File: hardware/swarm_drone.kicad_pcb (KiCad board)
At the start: 4 copper layers, 0 parts

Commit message: feat(kicad): Initial pcb layout
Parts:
- added C1: 100n, Capacitor_SMD:C_0402_1005Metric, F.Cu at (147.5, 106.1)
- added C10: 100n, Capacitor_SMD:C_0402_1005Metric, F.Cu at (175.4, 82.0)
- added C11: 2u2, Capacitor_SMD:C_0402_1005Metric, F.Cu at (145.5, 107.5)
- added C12: 2u2, Capacitor_SMD:C_0402_1005Metric, F.Cu at (178.2, 76.1)
- added C13: 10u, Capacitor_SMD:C_0603_1608Metric, F.Cu at (126.1, 104.0)
- added C14: 100n, Capacitor_SMD:C_0402_1005Metric, F.Cu at (120.9, 103.7)
- added C15: 10u, Capacitor_SMD:C_0603_1608Metric, F.Cu at (126.1, 106.0)
- added C16: 10n, Capacitor_SMD:C_0402_1005Metric, F.Cu at (122.5, 107.5)
- added C17: 0.1u, Capacitor_SMD:C_0402_1005Metric, F.Cu at (153.0, 95.2)
- added C18: 2.2u, Capacitor_SMD:C_0402_1005Metric, F.Cu at (154.1, 97.5)
- added C19: 10n, Capacitor_SMD:C_0402_1005Metric, F.Cu at (152.0, 95.2)
- added C2: 100n, Capacitor_SMD:C_0402_1005Metric, F.Cu at (173.0, 87.5)
- added C20: 100n, Capacitor_SMD:C_0402_1005Metric, F.Cu at (131.5, 103.0)
- added C21: 100n, Capacitor_SMD:C_0402_1005Metric, F.Cu at (133.7, 104.9)
- added C22: 26p, Capacitor_SMD:C_0402_1005Metric, F.Cu at (178.2, 78.0)
- added C23: 26p, Capacitor_SMD:C_0402_1005Metric, F.Cu at (178.2, 80.0)
- added C24: 100n, Capacitor_SMD:C_0402_1005Metric, B.Cu at (142.1, 101.6)
- added C25: 4u7, Capacitor_SMD:C_0603_1608Metric, B.Cu at (139.1, 99.5)
- added C26: 100n, Capacitor_SMD:C_0402_1005Metric, B.Cu at (144.6, 109.6)
- added C27: 4u7, Capacitor_SMD:C_0603_1608Metric, B.Cu at (146.1, 107.5)
- added C28: 33n, Capacitor_SMD:C_0402_1005Metric, F.Cu at (148.9, 71.0)
- added C29: 10n, Capacitor_SMD:C_0402_1005Metric, F.Cu at (148.9, 73.0)
- added C3: 100n, Capacitor_SMD:C_0402_1005Metric, F.Cu at (173.0, 89.5)
- added C30: 1n, Capacitor_SMD:C_0402_1005Metric, F.Cu at (141.0, 85.2)
- added C31: 2n2, Capacitor_SMD:C_0402_1005Metric, F.Cu at (151.7, 71.0)
- added C32: 4p7, Capacitor_SMD:C_0402_1005Metric, F.Cu at (151.7, 73.0)
- added C33: 1p5, Capacitor_SMD:C_0402_1005Metric, F.Cu at (151.0, 76.0)
- added C34: 1p, Capacitor_SMD:C_0402_1005Metric, F.Cu at (154.6, 71.0)
- added C35: 8p2, Capacitor_SMD:C_0402_1005Metric, F.Cu at (154.6, 73.0)
- added C36: 8p2, Capacitor_SMD:C_0402_1005Metric, F.Cu at (154.6, 74.9)
- added C4: 100n, Capacitor_SMD:C_0402_1005Metric, F.Cu at (173.0, 91.4)
- added C5: 100n, Capacitor_SMD:C_0402_1005Metric, F.Cu at (173.0, 93.4)
- added C6: 10u, Capacitor_SMD:C_0603_1608Metric, F.Cu at (182.2, 96.5)
- added C7: 10n, Capacitor_SMD:C_0402_1005Metric, F.Cu at (175.4, 76.1)
- added C8: 1u, Capacitor_SMD:C_0402_1005Metric, F.Cu at (175.4, 78.0)
- added C9: 1u, Capacitor_SMD:C_0402_1005Metric, F.Cu at (175.4, 80.0)
- added D1: D_Schottky, Diode_SMD:D_MicroSMP_LargeCathode, B.Cu at (127.0, 83.0)
- added D10: LED, LED_SMD:LED_0603_1608Metric, F.Cu at (154.5, 113.5)
- added D2: D_Schottky, Diode_SMD:D_MicroSMP_LargeCathode, B.Cu at (158.5, 82.1)
- added D3: D_Schottky, Diode_SMD:D_MicroSMP_LargeCathode, B.Cu at (126.0, 121.9)
- added D4: D_Schottky, Diode_SMD:D_MicroSMP_LargeCathode, B.Cu at (159.0, 121.4)
- added D5: LED, LED_SMD:LED_0603_1608Metric, F.Cu at (154.5, 103.5)
- added D6: LED, LED_SMD:LED_0603_1608Metric, F.Cu at (154.5, 105.5)
- added D7: LED, LED_SMD:LED_0603_1608Metric, F.Cu at (154.5, 107.5)
- added D8: LED, LED_SMD:LED_0603_1608Metric, F.Cu at (154.5, 109.5)
- added D9: LED, LED_SMD:LED_0603_1608Metric, F.Cu at (154.5, 111.5)
- added DWM1: DWM3000, RF_Module:DWM1000, F.Cu at (142.5, 122.0)
- added FB1: 120R, Inductor_SMD:L_0603_1608Metric, F.Cu at (182.2, 99.0)
- added J1: Conn_01x02_Pin, Connector_JST:JST_PH_S2B-PH-K_1x02_P2.00mm_Horizontal, B.Cu at (121.5, 100.5)
- added J2: Conn_01x03_Socket, Connector_PinHeader_1.00mm:PinHeader_1x03_P1.00mm_Horizontal, F.Cu at (163.0, 100.5)
- added J3: Conn_01x03_Socket, Connector_PinHeader_1.00mm:PinHeader_1x03_P1.00mm_Horizontal, F.Cu at (163.0, 96.5)
- added J5: Conn_01x02_Socket, Connector_JST:JST_ZH_B2B-ZR_1x02_P1.50mm_Vertical, B.Cu at (122.5, 81.8)
- added J6: Conn_01x02_Socket, Connector_JST:JST_ZH_B2B-ZR_1x02_P1.50mm_Vertical, B.Cu at (162.0, 81.5)
- added J7: Conn_01x02_Socket, Connector_JST:JST_ZH_B2B-ZR_1x02_P1.50mm_Vertical, B.Cu at (162.1, 120.8)
- added J8: Conn_01x02_Socket, Connector_JST:JST_ZH_B2B-ZR_1x02_P1.50mm_Vertical, B.Cu at (122.0, 120.8)
- added JP1: Jumper_2_Open, Jumper:SolderJumper-2_P1.3mm_Open_RoundedPad1.0x1.5mm, B.Cu at (138.0, 94.3)
- added JP2: Jumper_2_Open, Jumper:SolderJumper-2_P1.3mm_Open_RoundedPad1.0x1.5mm, B.Cu at (140.5, 94.3)
- added JP3: Jumper_2_Open, Jumper:SolderJumper-2_P1.3mm_Open_RoundedPad1.0x1.5mm, B.Cu at (143.0, 94.3)
- added JP4: Jumper_2_Open, Jumper:SolderJumper-2_P1.3mm_Open_RoundedPad1.0x1.5mm, B.Cu at (145.5, 94.3)
- added JP5: Jumper_2_Open, Jumper:SolderJumper-2_P1.3mm_Open_RoundedPad1.0x1.5mm, B.Cu at (148.0, 94.3)
- added JP6: Jumper_2_Open, Jumper:SolderJumper-2_P1.3mm_Open_RoundedPad1.0x1.5mm, B.Cu at (135.5, 94.3)
- added L1: 2n7, Inductor_SMD:L_0402_1005Metric, F.Cu at (157.5, 71.0)
- added L2: 3n9, Inductor_SMD:L_0402_1005Metric, F.Cu at (157.5, 73.0)
- added L3: 8n2, Inductor_SMD:L_0402_1005Metric, F.Cu at (157.5, 75.0)
- added Q1: AO3400A, Package_TO_SOT_SMD:SOT-23, B.Cu at (123.0, 87.5)
- added Q2: AO3400A, Package_TO_SOT_SMD:SOT-23, B.Cu at (162.7, 87.1)
- added Q3: AO3400A, Package_TO_SOT_SMD:SOT-23, B.Cu at (162.5, 116.5)
- added Q4: AO3400A, Package_TO_SOT_SMD:SOT-23, B.Cu at (122.5, 116.5)
- added R1: 10k, Resistor_SMD:R_0402_1005Metric, F.Cu at (139.1, 71.0)
- added R10: 2k2, Resistor_SMD:R_0402_1005Metric, F.Cu at (142.0, 71.0)
- added R11: 2k2, Resistor_SMD:R_0402_1005Metric, F.Cu at (150.0, 89.0)
- added R12: 10k, Resistor_SMD:R_0402_1005Metric, B.Cu at (126.0, 87.5)
- added R13: 10k, Resistor_SMD:R_0402_1005Metric, B.Cu at (160.0, 87.0)
- added R14: 10k, Resistor_SMD:R_0402_1005Metric, B.Cu at (159.5, 117.0)
- added R15: 10k, Resistor_SMD:R_0402_1005Metric, B.Cu at (125.0, 117.5)
- added R16: 10k, Resistor_SMD:R_0402_1005Metric, B.Cu at (140.1, 101.7)
- added R17: 10k, Resistor_SMD:R_0402_1005Metric, B.Cu at (144.0, 101.6)
- added R18: 10k, Resistor_SMD:R_0402_1005Metric, B.Cu at (141.1, 110.2)
- added R19: 10k, Resistor_SMD:R_0402_1005Metric, B.Cu at (134.6, 105.9)
- added R2: 10k, Resistor_SMD:R_0402_1005Metric, F.Cu at (139.1, 73.0)
- added R20: 22K, Resistor_SMD:R_0402_1005Metric, F.Cu at (116.0, 95.5)
- added R21: 100k, Resistor_SMD:R_0402_1005Metric, F.Cu at (179.6, 112.0)
- added R22: 330R, Resistor_SMD:R_0402_1005Metric, F.Cu at (157.0, 103.5)
- added R23: 330R, Resistor_SMD:R_0402_1005Metric, F.Cu at (157.0, 105.5)
- added R24: 330R, Resistor_SMD:R_0402_1005Metric, F.Cu at (157.0, 107.5)
- added R25: 330R, Resistor_SMD:R_0402_1005Metric, F.Cu at (157.0, 109.5)
- added R26: 330R, Resistor_SMD:R_0402_1005Metric, F.Cu at (157.0, 111.5)
- added R27: 330R, Resistor_SMD:R_0402_1005Metric, F.Cu at (157.0, 113.5)
- added R3: 3.57k, Resistor_SMD:R_0402_1005Metric, F.Cu at (124.5, 107.5)
- added R4: 1.15k, Resistor_SMD:R_0402_1005Metric, F.Cu at (124.5, 108.6)
- added R5: 10k, Resistor_SMD:R_0402_1005Metric, F.Cu at (124.4, 101.4)
- added R6: 33k, Resistor_SMD:R_0402_1005Metric, F.Cu at (124.4, 102.5)
- added R7: 10k, Resistor_SMD:R_0402_1005Metric, F.Cu at (149.9, 96.9)
- added R8: 2k2, Resistor_SMD:R_0402_1005Metric, B.Cu at (143.3, 97.4)
- added R9: 2k2, Resistor_SMD:R_0402_1005Metric, B.Cu at (141.3, 97.4)
- added SW1: SW_Push, Button_Switch_SMD:SW_Push_1P1T_NO_CK_KSC6xxG, F.Cu at (112.0, 110.5)
- added TP1: GND, TestPoint:TestPoint_Pad_D1.5mm, F.Cu at (169.3, 76.8)
- added TP2: I2C2_SCL, TestPoint:TestPoint_Pad_D1.5mm, F.Cu at (169.3, 80.4)
- added TP3: I2C2_SDA, TestPoint:TestPoint_Pad_D1.5mm, F.Cu at (169.3, 84.0)
- added TP4: +3V3, TestPoint:TestPoint_Pad_D1.5mm, F.Cu at (169.0, 87.5)
- added U1: STM32F405RGT7, Package_QFP:LQFP-64_10x10mm_P0.5mm, F.Cu at (142.3, 100.2)
- added U2: TPS7A91, Package_DFN_QFN:Texas_S-PDSO-N10_EP1.2x2mm, F.Cu at (123.0, 105.0)
- added U3: ICM-42688-P, ICM-42688-P:PQFN50P300X250X97-14N, F.Cu at (152.0, 98.0)
- added U4: BMP581, footprints:QFN10_BMP581_BOS, F.Cu at (133.5, 103.0)
- added U5: VL53L1CXV0FY1, Sensor_Distance:ST_VL53L1x, B.Cu at (142.7, 99.5)
- added U6: GD25Q128ESIGR, GD25Q128:SOP8_208MIL_GDV, B.Cu at (140.5, 106.5)
- added U7: nRF24L01P, Package_DFN_QFN:QFN-20-1EP_4x4mm_P0.5mm_EP2.5x2.5mm, F.Cu at (142.0, 88.5)
- added U8: NRF24L01_Breakout, RF_Module:nRF24L01_Breakout, B.Cu at (115.6, 70.3)
- added X1: 8MHz, abm:ABM3B_ABR, F.Cu at (133.3, 96.8)
- added Y1: 16MHz (C13738), Crystal:Crystal_SMD_3225-4Pin_3.2x2.5mm, F.Cu at (146.5, 88.0)
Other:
- board outline added: 45 x 45 mm

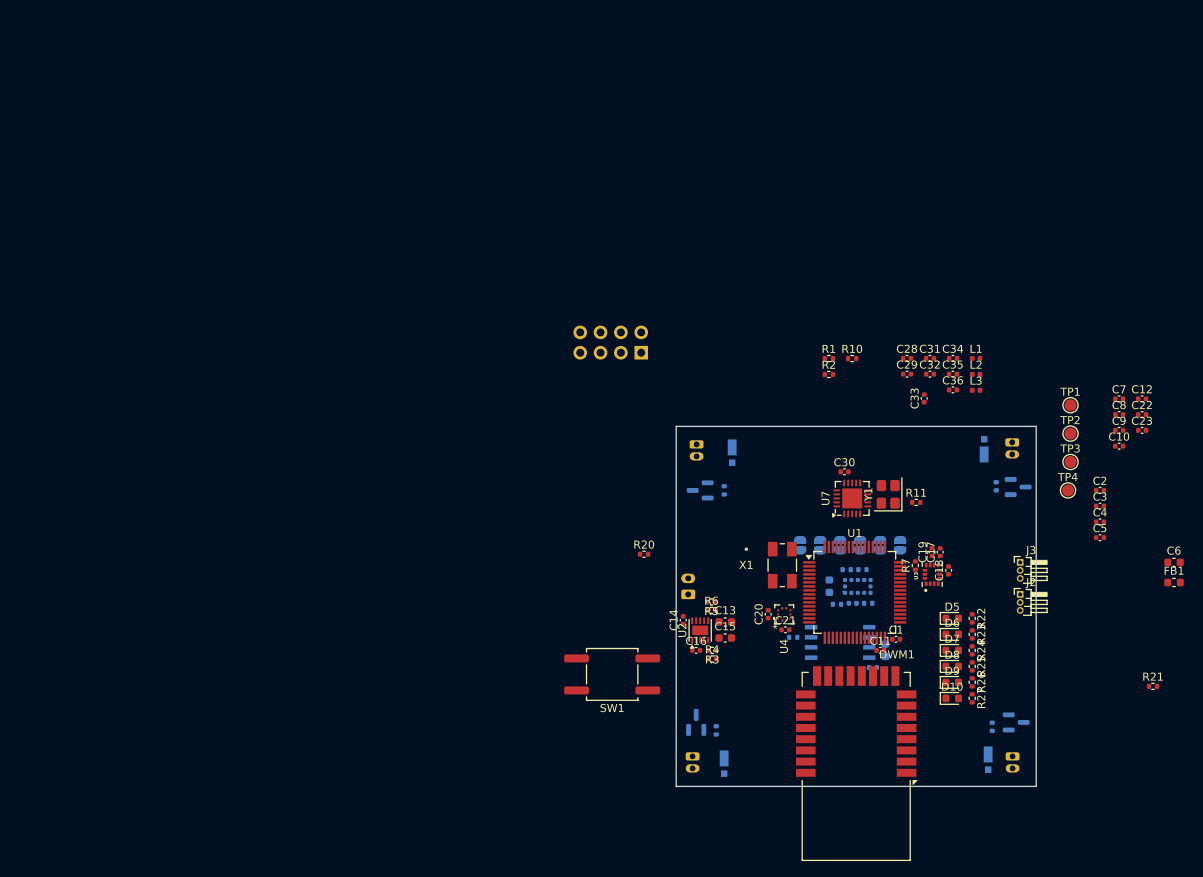
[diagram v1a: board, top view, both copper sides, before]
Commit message: feat(kicad): Added step files for missing parts
changed flyback diode to SMA part with 5A max

Redid initial layout
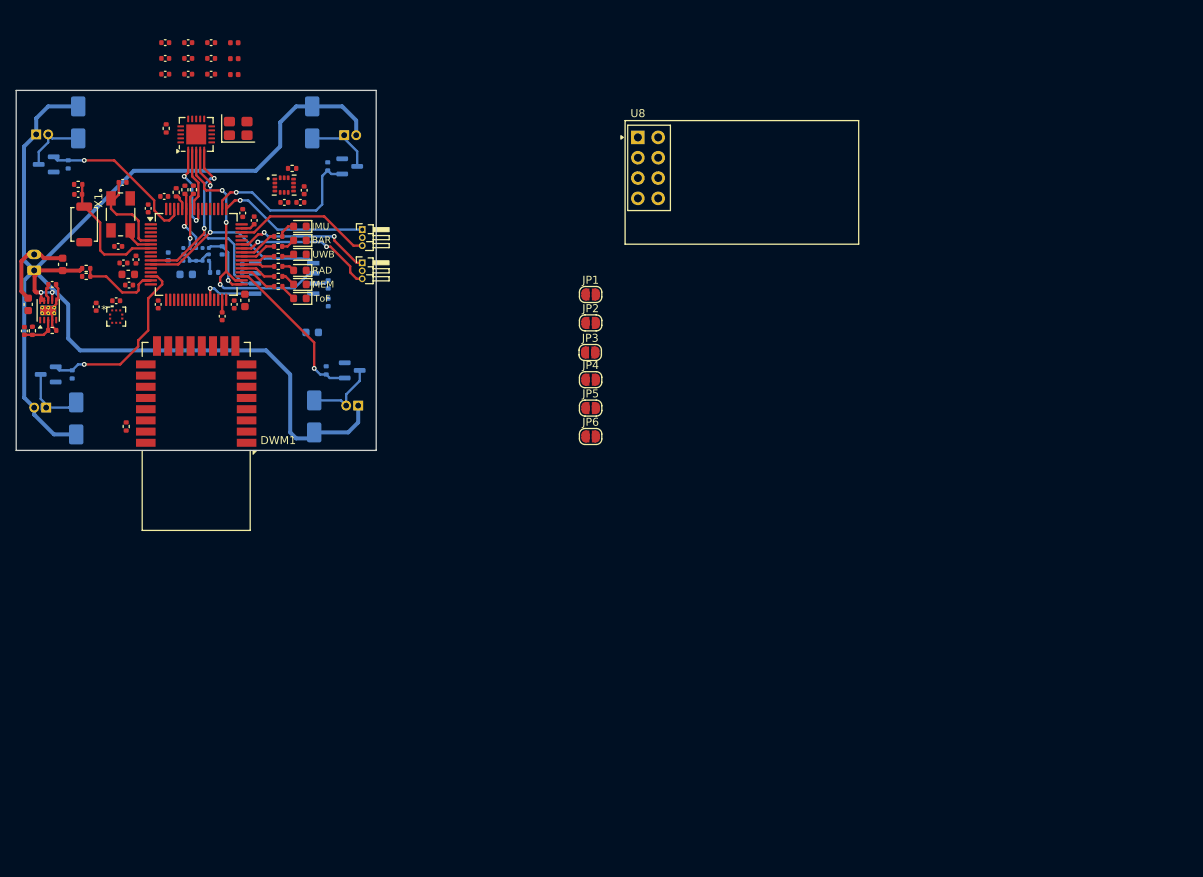
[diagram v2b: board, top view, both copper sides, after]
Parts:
- removed R10, R11: 2k2, Resistor_SMD:R_0402_1005Metric
- removed TP1: GND, TestPoint:TestPoint_Pad_D1.5mm
- removed TP2: I2C2_SCL, TestPoint:TestPoint_Pad_D1.5mm
- removed TP3: I2C2_SDA, TestPoint:TestPoint_Pad_D1.5mm
- removed TP4: +3V3, TestPoint:TestPoint_Pad_D1.5mm
- D1, D2, D3, D4: value D_Schottky -> D_Schottky (C22452); footprint Diode_SMD:D_MicroSMP_LargeCathode -> Diode_SMD:D_SMA
- J5, J6, J7, J8: footprint Connector_JST:JST_ZH_B2B-ZR_1x02_P1.50mm_Vertical -> MotorJST:JST_S2B-ZR-3.4_LF__SN_
- JP1, JP2, JP3, JP4, JP5, JP6, R8, R9, U8: moved to F.Cu
- SW1: footprint Button_Switch_SMD:SW_Push_1P1T_NO_CK_KSC6xxG -> Button_Switch_SMD:SW_SPST_TS-1088-xR020
- U2: footprint Package_DFN_QFN:Texas_S-PDSO-N10_EP1.2x2mm -> Package_DFN_QFN:Texas_S-PDSO-N10_EP1.2x2mm_ThermalVias
- moved FB1 136.3 mm to (51.5, 60.5), turned to 180 degrees
- moved C10 133.9 mm to (45.2, 50.5), turned to 180 degrees
- moved R21 132.4 mm to (51.2, 79.5), turned to -90 degrees
- moved C22 130.7 mm to (50.8, 49.0)
- moved C23 130.0 mm to (50.2, 57.0)
- moved C7 125.6 mm to (50.9, 59.1), turned to 180 degrees
- moved C9 125.1 mm to (51.6, 61.8), turned to 180 degrees
- moved C8 124.4 mm to (52.5, 58.6), turned to 90 degrees
- moved C4 123.9 mm to (56.0, 50.8)
- moved D4 121.8 mm to (45.0, 78.5), turned to 90 degrees
- moved C6 120.7 mm to (66.1, 63.8), turned to -90 degrees
- moved C2 120.0 mm to (55.2, 64.2), turned to 90 degrees
- moved C3 113.3 mm to (65.8, 52.8), turned to 90 degrees
- moved C12 113.2 mm to (67.2, 53.8), turned to -90 degrees
- moved C5 112.1 mm to (64.8, 64.2), turned to -90 degrees
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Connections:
- net Net-(U2-NR/SS) renamed /Power Regulation/NRSS
- C16 pad 1: +3V3 -> /Power Regulation/FB
- R3 pad 1: Net-(U2-FB) -> /Power Regulation/FB
- R4 pad 2: Net-(U2-FB) -> /Power Regulation/FB
- U1 pad 29: /Microcontroller/I2C2_SCL -> unconnected-(U1-PB10-Pad29)
- U1 pad 30: /Microcontroller/I2C2_SDA -> unconnected-(U1-PB11-Pad30)
- U2 pad 3: Net-(U2-FB) -> /Power Regulation/FB
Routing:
- net +BATT: track 0.00 -> 177.8 mm, vias 0 -> 2
- net /Barometer/SPI2_SCK: track 0.00 -> 34.8 mm, vias 0 -> 3
- net /Barometer/SPI2_MOSI: track 0.00 -> 34.4 mm, vias 0 -> 2
- net /Barometer/SPI2_MISO: track 0.00 -> 32.0 mm, vias 0 -> 2
- net /Microcontroller/M4: track 0.00 -> 22.8 mm, vias 0 -> 1
- net /Microcontroller/M2: track 0.00 -> 21.7 mm, vias 0 -> 1
- net GND: track 0.00 -> 21.5 mm
- net /Microcontroller/M1: track 0.00 -> 20.2 mm, vias 0 -> 1
- net /Microcontroller/M3: track 0.00 -> 20.0 mm, vias 0 -> 1
- net /Microcontroller/SWCLK: track 0.00 -> 19.0 mm, vias 0 -> 1
- net /Microcontroller/USART1_TX: track 0.00 -> 17.8 mm, vias 0 -> 2
- net /Microcontroller/USART1_RX: track 0.00 -> 17.6 mm, vias 0 -> 2
- net /Microcontroller/SWDIO: track 0.00 -> 17.4 mm
- net /Microcontroller/NRST: track 0.00 -> 15.8 mm
- net /Microcontroller/HSE_IN: track 0.00 -> 11.4 mm
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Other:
- board text added: "BAR"
- board text added: "IMU"
- board text added: "MEM"
- board text added: "RAD"
- board text added: "ToF"
- board text added: "UWB"

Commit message: feat(kicad): Updated schematic to keep traces shorter on the layout Restarting layout
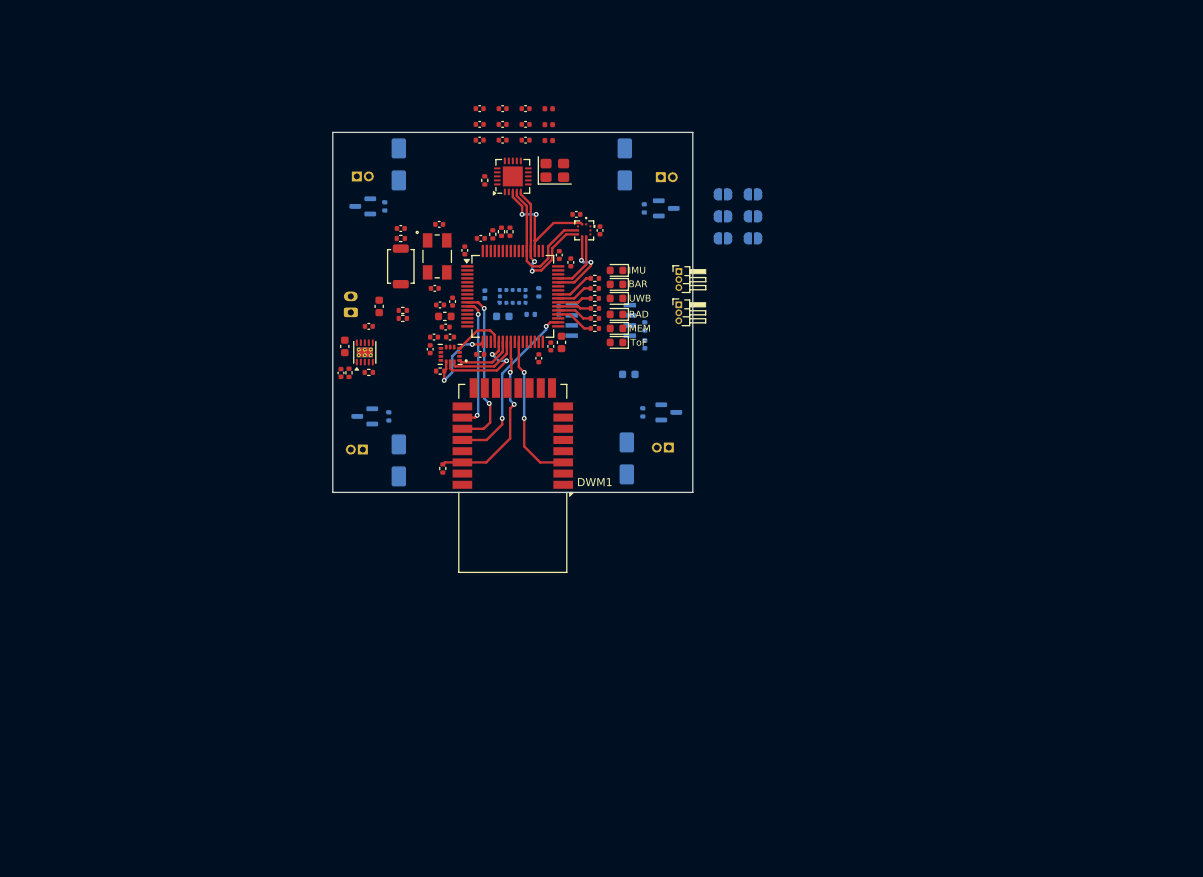
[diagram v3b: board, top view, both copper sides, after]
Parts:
- removed U8: NRF24L01_Breakout, RF_Module:nRF24L01_Breakout
- JP1, JP2, JP3, JP4, JP5, JP6: moved to B.Cu
- moved C20 61.1 mm to (107.5, 53.0), turned to 180 degrees
- moved C21 61.1 mm to (110.5, 55.0), turned to -90 degrees
- moved U4 59.5 mm to (108.5, 55.0), turned to -90 degrees
- moved R2 40.9 mm to (85.6, 56.0), turned to 0 degrees
- moved C2 40.7 mm to (95.5, 70.5), turned to 180 degrees
- moved D4 40.7 mm to (85.3, 83.8)
- moved C10 40.5 mm to (85.6, 54.8), turned to 0 degrees
- moved D1 40.4 mm to (85.3, 46.8)
- moved J5 40.4 mm to (80.8, 46.6)
- moved R20 40.4 mm to (96.1, 48.8)
- moved C31 40.2 mm to (98.3, 39.8)
- moved C32 40.2 mm to (98.3, 41.8)
- moved C33 40.2 mm to (98.3, 43.7)
- moved C28 40.2 mm to (95.4, 39.8)
- moved C29 40.2 mm to (95.4, 41.8)
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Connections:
- DWM1 pad 18: /Barometer/SPI2_MOSI -> /Flash Memory/SPI2_MOSI
- DWM1 pad 19: /Barometer/SPI2_MISO -> /Flash Memory/SPI2_MISO
- DWM1 pad 20: /Barometer/SPI2_SCK -> /Flash Memory/SPI2_SCK
- JP1 pad 1: /Microcontroller/SPI3_MISO -> /Barometer/SPI3_MISO
- JP1 pad 2: /Radio/SPI3_MISO -> unconnected-(JP1-B-Pad2)
- JP2 pad 1: /Microcontroller/SPI3_MOSI -> /Barometer/SPI3_MOSI
- JP2 pad 2: /Radio/SPI3_MOSI -> unconnected-(JP2-B-Pad2)
- JP3 pad 1: /Microcontroller/SPI3_SCK -> /Barometer/SPI3_SCK
- JP3 pad 2: /Radio/SPI3_SCK -> unconnected-(JP3-B-Pad2)
- JP4 pad 2: /Radio/RADIO_ALT_CE -> unconnected-(JP4-B-Pad2)
- JP5 pad 2: /Radio/RADIO_ALT_CS -> unconnected-(JP5-B-Pad2)
- JP6 pad 2: /Radio/RADIO_ALT_INT -> unconnected-(JP6-B-Pad2)
- U1 pad 10: /Barometer/SPI2_MISO -> /Flash Memory/SPI2_MISO
- U1 pad 11: /Barometer/SPI2_MOSI -> /Flash Memory/SPI2_MOSI
- U1 pad 17: unconnected-(U1-PA3-Pad17) -> /IMU/IMU_CS
- U1 pad 20: unconnected-(U1-PA4-Pad20) -> /IMU/IMU_INT
- U1 pad 34: /Barometer/SPI2_SCK -> /Flash Memory/SPI2_SCK
- U1 pad 44: /IMU/IMU_CS -> /Barometer/BARO_CS
- U1 pad 45: /IMU/IMU_INT -> /Barometer/BARO_INT
- U1 pad 51: /Microcontroller/SPI3_SCK -> /Barometer/SPI3_SCK
- U1 pad 52: /Microcontroller/SPI3_MISO -> /Barometer/SPI3_MISO
- U1 pad 53: /Microcontroller/SPI3_MOSI -> /Barometer/SPI3_MOSI
- U1 pad 8: /Barometer/BARO_INT -> unconnected-(U1-PC0-Pad8)
- U1 pad 9: /Barometer/BARO_CS -> unconnected-(U1-PC1-Pad9)
- U4 pad 2: /Barometer/SPI2_SCK -> /Barometer/SPI3_SCK
- U4 pad 4: /Barometer/SPI2_MOSI -> /Barometer/SPI3_MOSI
- U4 pad 5: /Barometer/SPI2_MISO -> /Barometer/SPI3_MISO
- U6 pad 2: /Barometer/SPI2_MISO -> /Flash Memory/SPI2_MISO
- U6 pad 5: /Barometer/SPI2_MOSI -> /Flash Memory/SPI2_MOSI
- U6 pad 6: /Barometer/SPI2_SCK -> /Flash Memory/SPI2_SCK
- U7 pad 3: /Barometer/SPI2_SCK -> /Barometer/SPI3_SCK
- U7 pad 4: /Barometer/SPI2_MOSI -> /Barometer/SPI3_MOSI
- U7 pad 5: /Barometer/SPI2_MISO -> /Barometer/SPI3_MISO
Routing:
- net +BATT: track 177.8 -> 0.00 mm, vias 2 -> 0
- net /Barometer/SPI2_SCK: track 34.8 -> 0.00 mm, vias 3 -> 0
- net /Barometer/SPI2_MOSI: track 34.4 -> 0.00 mm, vias 2 -> 0
- net /Barometer/SPI2_MISO: track 32.0 -> 0.00 mm, vias 2 -> 0
- net /Microcontroller/M4: track 22.8 -> 0.00 mm, vias 1 -> 0
- net /Microcontroller/UWB_INT: track 0.00 -> 22.4 mm, vias 0 -> 2
- net /Flash Memory/SPI2_SCK: track 0.00 -> 22.0 mm, vias 0 -> 2
- net /Microcontroller/M2: track 21.7 -> 0.00 mm, vias 1 -> 0
- net GND: track 21.5 -> 0.00 mm
- net /Flash Memory/SPI2_MISO: track 0.00 -> 20.8 mm, vias 0 -> 2
- net /Microcontroller/M1: track 20.2 -> 0.00 mm, vias 1 -> 0
- net /Microcontroller/M3: track 20.0 -> 0.00 mm, vias 1 -> 0
- net /Barometer/SPI3_MISO: track 0.00 -> 19.3 mm, vias 0 -> 2
- net /Microcontroller/UWB_RESET: track 0.00 -> 19.1 mm, vias 0 -> 2
- net /Microcontroller/SWCLK: track 19.0 -> 0.00 mm, vias 1 -> 0
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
